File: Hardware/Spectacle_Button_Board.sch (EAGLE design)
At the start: 46 parts, among them J17 AUDIO-JACK3, J19 FTDI_DEVICE, U1 CY8C4146LQI-S422, U2 MIC5205-5V

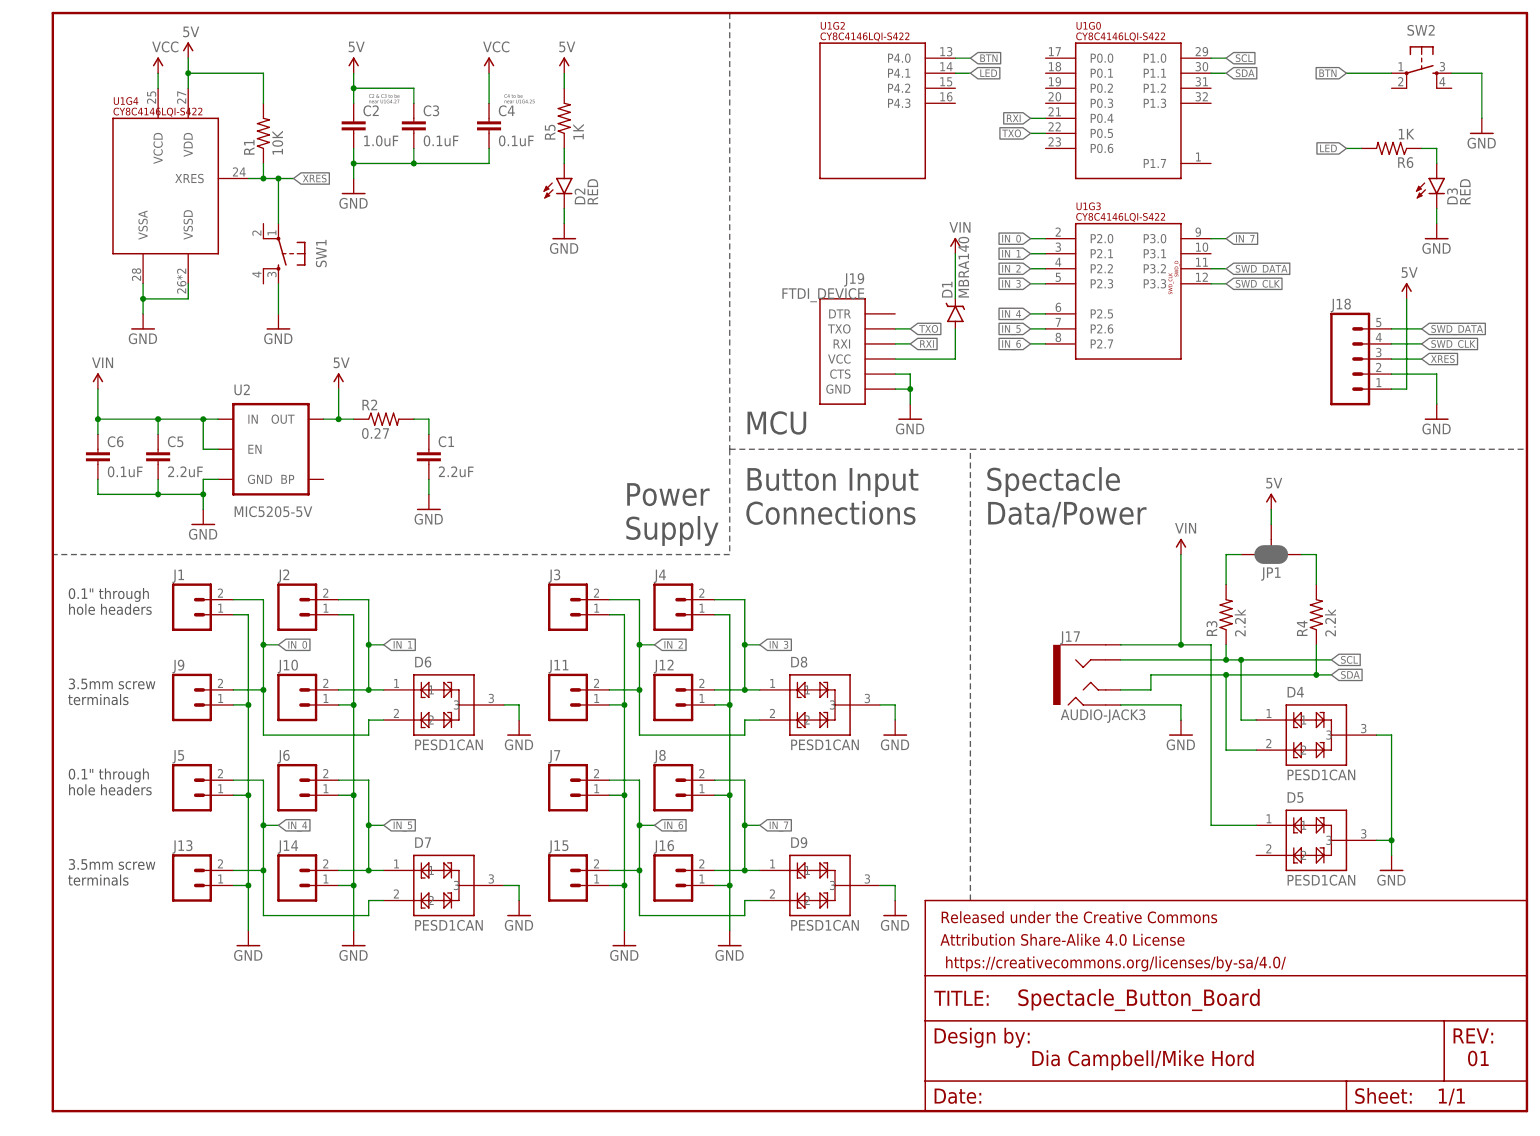
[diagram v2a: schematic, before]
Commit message: Adjust to 3.3V
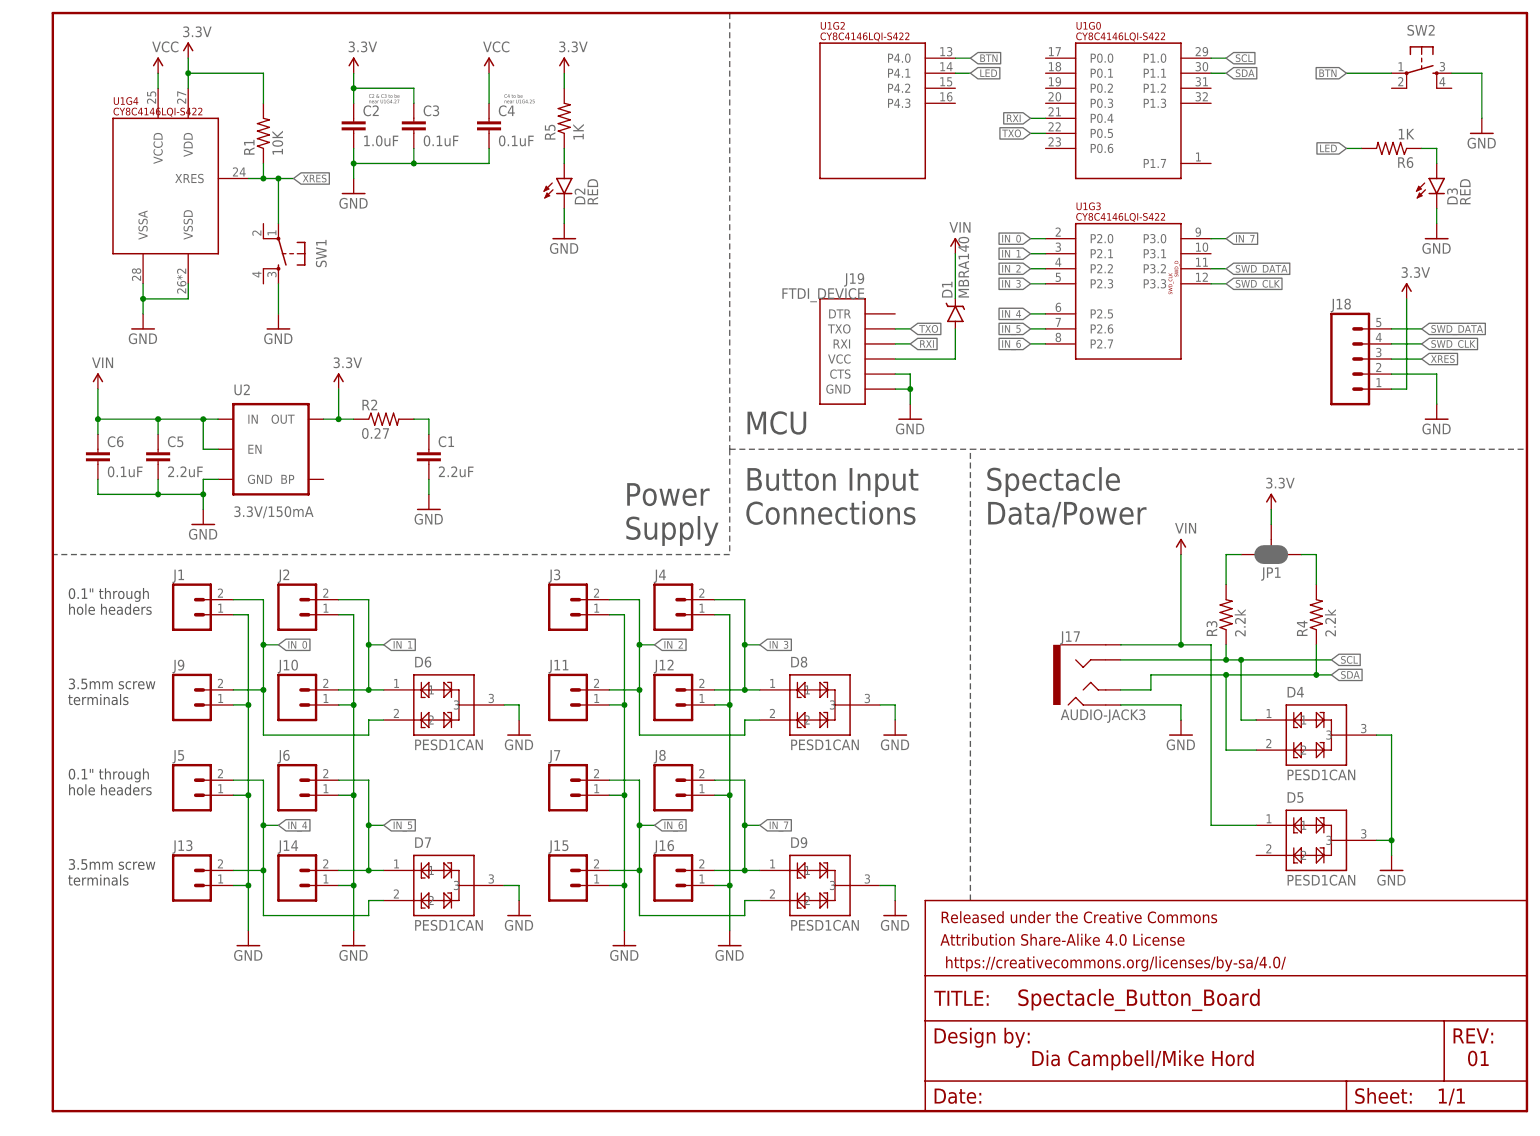
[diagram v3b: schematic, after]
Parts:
- U2: value MIC5205-5V -> 3.3V/150mA; device SparkFun-PowerIC:V_REG_MIC52055V -> SparkFun-PowerIC:V_REG_MIC52053.3V
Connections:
- net 5V renamed 3.3V
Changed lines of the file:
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@@
 <part name="FRAME1" library="SparkFun-Aesthetics" deviceset="FRAME-LETTER" device=""/>
 <part name="U1" library="SparkFun-DigitalIC" deviceset="PSOC4_4100S_32QFN" device="" value="CY8C4146LQI-S422"/>
-<part name="SUPPLY1" library="SparkFun-Aesthetics" deviceset="5V" device=""/>
 <part name="GND1" library="SparkFun-Aesthetics" deviceset="GND" device=""/>
 <part name="SUPPLY2" library="SparkFun-Aesthetics" deviceset="VIN" device=""/>
-<part name="U2" library="SparkFun-PowerIC" deviceset="V_REG_MIC5205" device="5V" value="MIC5205-5V"/>
+<part name="U2" library="SparkFun-PowerIC" deviceset="V_REG_MIC5205" device="3.3V" value="3.3V/150mA"/>
 <part name="J1" library="SparkFun-Connectors" deviceset="M02" device="PTH"/>
 <part name="J2" library="SparkFun-Connectors" deviceset="M02" device="PTH"/>
@@
 <part name="SUPPLY3" library="SparkFun-Aesthetics" deviceset="VCC" device=""/>
 <part name="R1" library="SparkFun-Resistors" deviceset="10KOHM-1/10W-1%(0603)" device="0603" value="10K"/>
-<part name="SUPPLY4" library="SparkFun-Aesthetics" deviceset="5V" device=""/>
 <part name="GND7" library="SparkFun-Aesthetics" deviceset="GND" device=""/>
 <part name="R2" library="SparkFun-Resistors" deviceset="0.27OHM-1/10W-1%(0603)" device="" value="0.27"/>
@@
 <part name="C3" library="SparkFun-Capacitors" deviceset="0.1UF-16V(+-10%)(0402)" device="" value="0.1uF"/>
 <part name="C4" library="SparkFun-Capacitors" deviceset="0.1UF-16V(+-10%)(0402)" device="" value="0.1uF"/>
-<part name="SUPPLY5" library="SparkFun-Aesthetics" deviceset="5V" device=""/>
 <part name="SUPPLY6" library="SparkFun-Aesthetics" deviceset="VCC" device=""/>
 <part name="GND8" library="SparkFun-Aesthetics" deviceset="GND" device=""/>
@@
 <part name="R4" library="SparkFun-Resistors" deviceset="2.2KOHM-1/10W-1%(0603)" device="" value="2.2k"/>
 <part name="JP1" library="SparkFun-Passives" deviceset="JUMPER-PAD-3-NC_BY_PASTE" device=""/>
-<part name="SUPPLY8" library="SparkFun-Aesthetics" deviceset="5V" device=""/>
 <part name="J18" library="SparkFun-Connectors" deviceset="M05" device="PTH"/>
 <part name="GND10" library="SparkFun-Aesthetics" deviceset="GND" device=""/>
-<part name="SUPPLY9" library="SparkFun-Aesthetics" deviceset="5V" device=""/>
 <part name="J19" library="SparkFun-Connectors" deviceset="FTDI_DEVICE" device=""/>
 <part name="D1" library="SparkFun-DiscreteSemi" deviceset="DIODE-SCHOTTKY" device="-MBRA140" value="MBRA140"/>
@@
 <part name="GND14" library="SparkFun-Aesthetics" deviceset="GND" device=""/>
 <part name="R6" library="SparkFun-Resistors" deviceset="1KOHM-1/10W-1%(0603)" device="" value="1K"/>
-<part name="SUPPLY11" library="SparkFun-Aesthetics" deviceset="5V" device=""/>
 <part name="GND15" library="SparkFun-Aesthetics" deviceset="GND" device=""/>
 <part name="J17" library="SparkFun-Connectors" deviceset="AUDIO-JACK3" device=""/>
@@
 <part name="GND19" library="SparkFun-Aesthetics" deviceset="GND" device=""/>
 <part name="GND20" library="SparkFun-Aesthetics" deviceset="GND" device=""/>
+<part name="SUPPLY1" library="SparkFun-Aesthetics" deviceset="3.3V" device=""/>
+<part name="SUPPLY4" library="SparkFun-Aesthetics" deviceset="3.3V" device=""/>
+<part name="SUPPLY5" library="SparkFun-Aesthetics" deviceset="3.3V" device=""/>
+<part name="SUPPLY12" library="SparkFun-Aesthetics" deviceset="3.3V" device=""/>
+<part name="SUPPLY13" library="SparkFun-Aesthetics" deviceset="3.3V" device=""/>
+<part name="SUPPLY14" library="SparkFun-Aesthetics" deviceset="3.3V" device=""/>
 </parts>
 <sheets>
@@
 <instance part="U1" gate="G3" x="172.72" y="127"/>
 <instance part="U1" gate="G4" x="10.16" y="144.78"/>
-<instance part="SUPPLY1" gate="G$1" x="22.86" y="177.8"/>
 <instance part="GND1" gate="1" x="25.4" y="99.06"/>
 <instance part="SUPPLY2" gate="G$1" x="7.62" y="121.92"/>
@@
 <instance part="SUPPLY3" gate="G$1" x="17.78" y="175.26"/>
 <instance part="R1" gate="G$1" x="35.56" y="165.1" rot="R90"/>
-<instance part="SUPPLY4" gate="G$1" x="48.26" y="121.92"/>
 <instance part="GND7" gate="1" x="63.5" y="101.6"/>
 <instance part="R2" gate="G$1" x="55.88" y="116.84"/>
@@
 <instance part="C3" gate="G$1" x="60.96" y="165.1"/>
 <instance part="C4" gate="G$1" x="73.66" y="165.1"/>
-<instance part="SUPPLY5" gate="G$1" x="50.8" y="175.26"/>
 <instance part="SUPPLY6" gate="G$1" x="73.66" y="175.26"/>
 <instance part="GND8" gate="1" x="50.8" y="154.94"/>
@@
 <attribute name="NAME" x="207.518" y="91.821" size="1.778" layer="95" rot="R180"/>
 </instance>
-<instance part="SUPPLY8" gate="G$1" x="205.74" y="101.6"/>
 <instance part="J18" gate="G$1" x="218.44" y="127"/>
 <instance part="GND10" gate="1" x="233.68" y="116.84"/>
-<instance part="SUPPLY9" gate="G$1" x="228.6" y="137.16"/>
 <instance part="J19" gate="G$1" x="137.16" y="129.54" rot="MR0"/>
 <instance part="D1" gate="G$1" x="152.4" y="134.62" rot="R90"/>
@@
 <instance part="GND14" gate="1" x="241.3" y="165.1"/>
 <instance part="R6" gate="G$1" x="226.06" y="162.56" rot="R180"/>
-<instance part="SUPPLY11" gate="G$1" x="86.36" y="175.26"/>
 <instance part="GND15" gate="1" x="38.1" y="132.08"/>
 <instance part="J17" gate="G$1" x="175.26" y="73.66"/>
@@
 <instance part="GND19" gate="1" x="78.74" y="63.5"/>
 <instance part="GND20" gate="1" x="226.06" y="40.64"/>
+<instance part="SUPPLY1" gate="G$1" x="22.86" y="177.8"/>
+<instance part="SUPPLY4" gate="G$1" x="50.8" y="175.26"/>
+<instance part="SUPPLY5" gate="G$1" x="86.36" y="175.26"/>
+<instance part="SUPPLY12" gate="G$1" x="48.26" y="121.92"/>
+<instance part="SUPPLY13" gate="G$1" x="205.74" y="101.6"/>
+<instance part="SUPPLY14" gate="G$1" x="228.6" y="137.16"/>
 </instances>
 <busses>
@@
 </segment>
 </net>
-<net name="5V" class="0">
-<segment>
-<pinref part="SUPPLY1" gate="G$1" pin="5V"/>
-<pinref part="U1" gate="G4" pin="VDD"/>
-<wire x1="22.86" y1="177.8" x2="22.86" y2="175.26" width="0.1524" layer="91"/>
-<pinref part="R1" gate="G$1" pin="2"/>
-<wire x1="22.86" y1="175.26" x2="22.86" y2="172.72" width="0.1524" layer="91"/>
-<wire x1="22.86" y1="175.26" x2="35.56" y2="175.26" width="0.1524" layer="91"/>
-<wire x1="35.56" y1="175.26" x2="35.56" y2="170.18" width="0.1524" layer="91"/>
-<junction x="22.86" y="175.26"/>
-</segment>
-<segment>
-<pinref part="U2" gate="U1" pin="OUT"/>
-<pinref part="SUPPLY4" gate="G$1" pin="5V"/>
-<wire x1="45.72" y1="116.84" x2="48.26" y2="116.84" width="0.1524" layer="91"/>
-<wire x1="48.26" y1="116.84" x2="48.26" y2="121.92" width="0.1524" layer="91"/>
-<pinref part="R2" gate="G$1" pin="1"/>
-<wire x1="48.26" y1="116.84" x2="50.8" y2="116.84" width="0.1524" layer="91"/>
-<junction x="48.26" y="116.84"/>
-</segment>
-<segment>
-<pinref part="SUPPLY5" gate="G$1" pin="5V"/>
-<pinref part="C2" gate="G$1" pin="1"/>
-<wire x1="50.8" y1="175.26" x2="50.8" y2="172.72" width="0.1524" layer="91"/>
-<pinref part="C3" gate="G$1" pin="1"/>
-<wire x1="50.8" y1="172.72" x2="50.8" y2="170.18" width="0.1524" layer="91"/>
-<wire x1="50.8" y1="172.72" x2="60.96" y2="172.72" width="0.1524" layer="91"/>
-<wire x1="60.96" y1="172.72" x2="60.96" y2="170.18" width="0.1524" layer="91"/>
-<junction x="50.8" y="172.72"/>
-</segment>
-<segment>
-<pinref part="SUPPLY8" gate="G$1" pin="5V"/>
-<pinref part="JP1" gate="G$1" pin="2"/>
-<wire x1="205.74" y1="101.6" x2="205.74" y2="99.06" width="0.1524" layer="91"/>
-</segment>
-<segment>
-<pinref part="SUPPLY9" gate="G$1" pin="5V"/>
-<wire x1="228.6" y1="137.16" x2="228.6" y2="121.92" width="0.1524" layer="91"/>
-<pinref part="J18" gate="G$1" pin="1"/>
-<wire x1="228.6" y1="121.92" x2="226.06" y2="121.92" width="0.1524" layer="91"/>
-</segment>
-<segment>
-<pinref part="SUPPLY11" gate="G$1" pin="5V"/>
-<pinref part="R5" gate="G$1" pin="2"/>
-<wire x1="86.36" y1="175.26" x2="86.36" y2="172.72" width="0.1524" layer="91"/>
-</segment>
-</net>
 <net name="VCC" class="0">
 <segment>
@@
 </segment>
 </net>
+<net name="3.3V" class="0">
+<segment>
+<pinref part="U1" gate="G4" pin="VDD"/>
+<wire x1="22.86" y1="177.8" x2="22.86" y2="175.26" width="0.1524" layer="91"/>
+<pinref part="R1" gate="G$1" pin="2"/>
+<wire x1="22.86" y1="175.26" x2="22.86" y2="172.72" width="0.1524" layer="91"/>
+<wire x1="22.86" y1="175.26" x2="35.56" y2="175.26" width="0.1524" layer="91"/>
+<wire x1="35.56" y1="175.26" x2="35.56" y2="170.18" width="0.1524" layer="91"/>
+<junction x="22.86" y="175.26"/>
+<pinref part="SUPPLY1" gate="G$1" pin="3.3V"/>
+</segment>
+<segment>
+<pinref part="C2" gate="G$1" pin="1"/>
+<wire x1="50.8" y1="175.26" x2="50.8" y2="172.72" width="0.1524" layer="91"/>
+<pinref part="C3" gate="G$1" pin="1"/>
+<wire x1="50.8" y1="172.72" x2="50.8" y2="170.18" width="0.1524" layer="91"/>
+<wire x1="50.8" y1="172.72" x2="60.96" y2="172.72" width="0.1524" layer="91"/>
+<wire x1="60.96" y1="172.72" x2="60.96" y2="170.18" width="0.1524" layer="91"/>
+<junction x="50.8" y="172.72"/>
+<pinref part="SUPPLY4" gate="G$1" pin="3.3V"/>
+</segment>
+<segment>
+<pinref part="U2" gate="U1" pin="OUT"/>
+<wire x1="45.72" y1="116.84" x2="48.26" y2="116.84" width="0.1524" layer="91"/>
+<wire x1="48.26" y1="116.84" x2="48.26" y2="121.92" width="0.1524" layer="91"/>
+<pinref part="R2" gate="G$1" pin="1"/>
+<wire x1="48.26" y1="116.84" x2="50.8" y2="116.84" width="0.1524" layer="91"/>
+<junction x="48.26" y="116.84"/>
+<pinref part="SUPPLY12" gate="G$1" pin="3.3V"/>
+</segment>
+<segment>
+<wire x1="228.6" y1="137.16" x2="228.6" y2="121.92" width="0.1524" layer="91"/>
+<pinref part="J18" gate="G$1" pin="1"/>
+<wire x1="228.6" y1="121.92" x2="226.06" y2="121.92" width="0.1524" layer="91"/>
+<pinref part="SUPPLY14" gate="G$1" pin="3.3V"/>
+</segment>
+<segment>
+<pinref part="JP1" gate="G$1" pin="2"/>
+<wire x1="205.74" y1="101.6" x2="205.74" y2="99.06" width="0.1524" layer="91"/>
+<pinref part="SUPPLY13" gate="G$1" pin="3.3V"/>
+</segment>
+<segment>
+<pinref part="R5" gate="G$1" pin="2"/>
+<wire x1="86.36" y1="175.26" x2="86.36" y2="172.72" width="0.1524" layer="91"/>
+<pinref part="SUPPLY5" gate="G$1" pin="3.3V"/>
+</segment>
+</net>

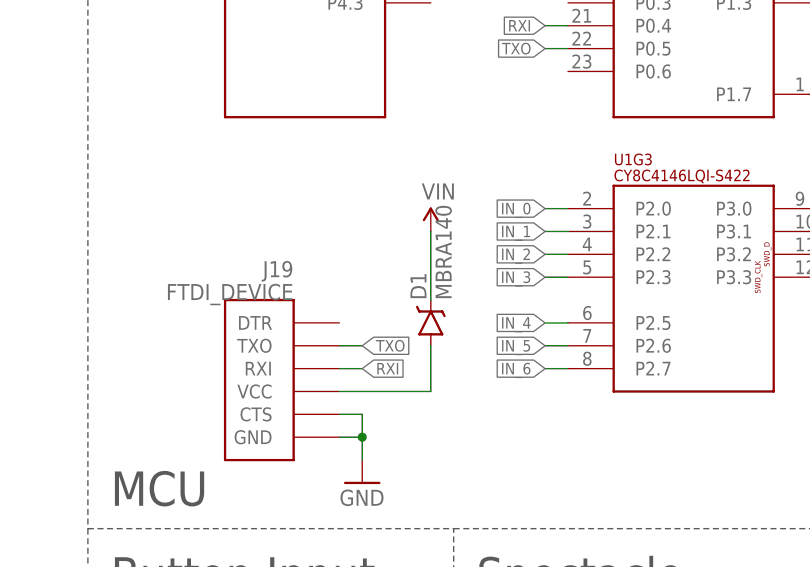
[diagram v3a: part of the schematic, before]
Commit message: Remove diode from serial port to VIN
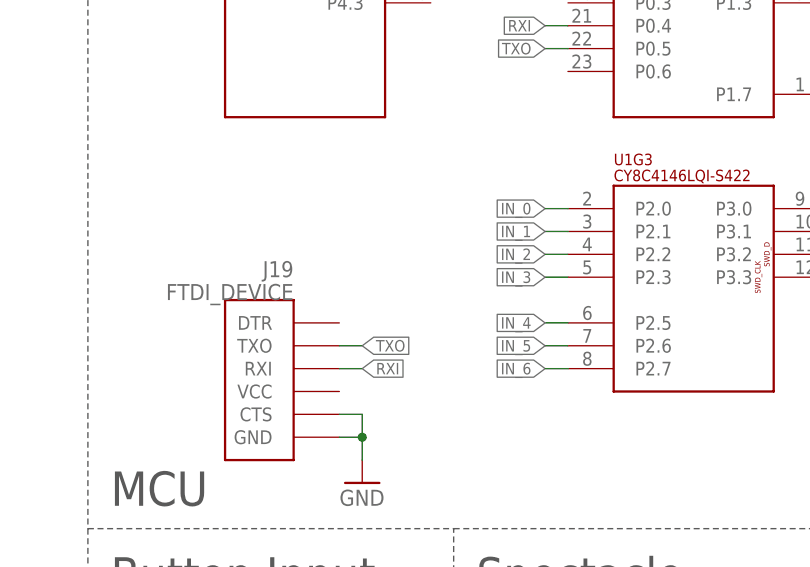
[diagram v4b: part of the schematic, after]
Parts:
- removed D1: MBRA140, SparkFun-DiscreteSemi:DIODE-SCHOTTKY-MBRA140
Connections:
- removed net N$1: D1.A, J19.VCC
- net VIN: no longer D1.C
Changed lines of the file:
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@@
 <part name="GND10" library="SparkFun-Aesthetics" deviceset="GND" device=""/>
 <part name="J19" library="SparkFun-Connectors" deviceset="FTDI_DEVICE" device=""/>
-<part name="D1" library="SparkFun-DiscreteSemi" deviceset="DIODE-SCHOTTKY" device="-MBRA140" value="MBRA140"/>
-<part name="SUPPLY10" library="SparkFun-Aesthetics" deviceset="VIN" device=""/>
 <part name="GND11" library="SparkFun-Aesthetics" deviceset="GND" device=""/>
 <part name="D2" library="SparkFun-LED" deviceset="LED-RED" device="0603" value="RED"/>
@@
 <instance part="GND10" gate="1" x="233.68" y="116.84"/>
 <instance part="J19" gate="G$1" x="137.16" y="129.54" rot="MR0"/>
-<instance part="D1" gate="G$1" x="152.4" y="134.62" rot="R90"/>
-<instance part="SUPPLY10" gate="G$1" x="152.4" y="144.78"/>
 <instance part="GND11" gate="1" x="144.78" y="116.84"/>
 <instance part="D2" gate="G$1" x="86.36" y="157.48"/>
@@
 <wire x1="195.58" y1="48.26" x2="203.2" y2="48.26" width="0.1524" layer="91"/>
 </segment>
-<segment>
-<pinref part="D1" gate="G$1" pin="C"/>
-<pinref part="SUPPLY10" gate="G$1" pin="VIN"/>
-<wire x1="152.4" y1="137.16" x2="152.4" y2="144.78" width="0.1524" layer="91"/>
-</segment>
 </net>
 <net name="N$2" class="0">
@@
 </segment>
 </net>
-<net name="N$1" class="0">
-<segment>
-<pinref part="J19" gate="G$1" pin="VCC"/>
-<pinref part="D1" gate="G$1" pin="A"/>
-<wire x1="142.24" y1="127" x2="152.4" y2="127" width="0.1524" layer="91"/>
-<wire x1="152.4" y1="127" x2="152.4" y2="132.08" width="0.1524" layer="91"/>
-</segment>
-</net>
